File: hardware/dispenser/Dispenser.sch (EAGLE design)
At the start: 59 parts, among them J1 AVR_Prog, J2 RJ45-8PTH, Q1 NFET-SO8, Q2 NFET, Q3 NFET, Q4 NFET, U1 ATMEGA168, U10 HALL-EFFECT, U2 OPAMP-DUAL, U3 OPTO-TLP185, U4 MPX10DP, U5 VREG-5V-LDO-AP1117SOT89-3L, U6 WS2801, U7 HALL-EFFECT, U8 HALL-EFFECT, U9 HALL-EFFECT

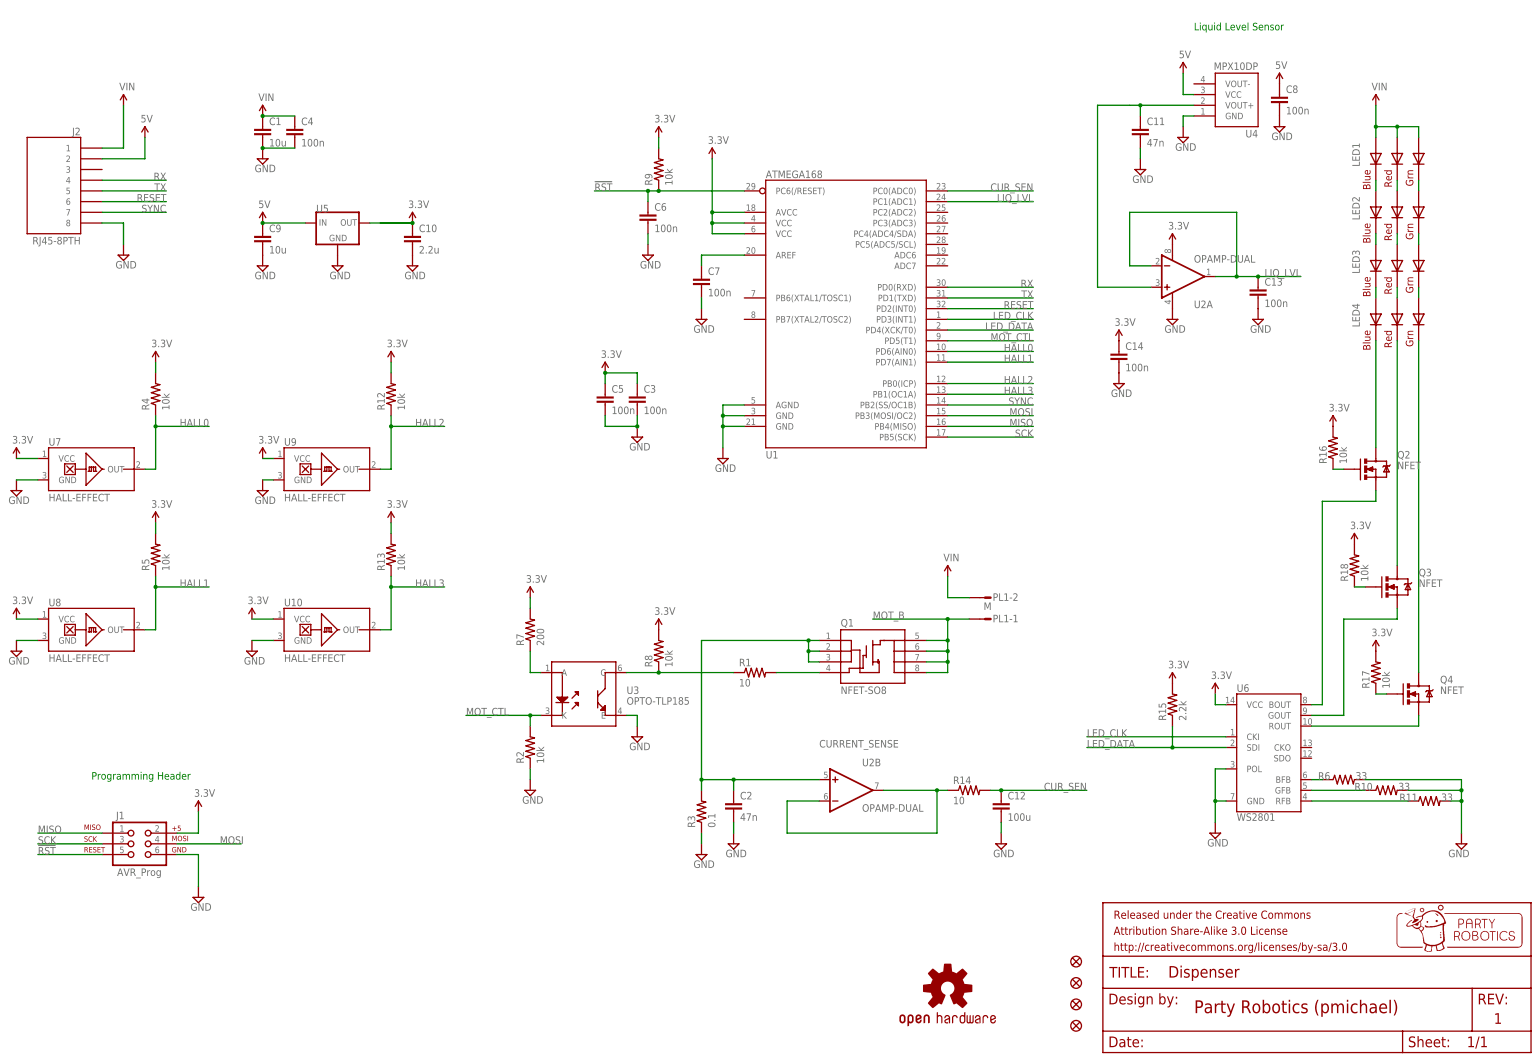
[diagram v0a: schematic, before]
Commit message: Updated Router Schematic with DS1307 and Accessory Port
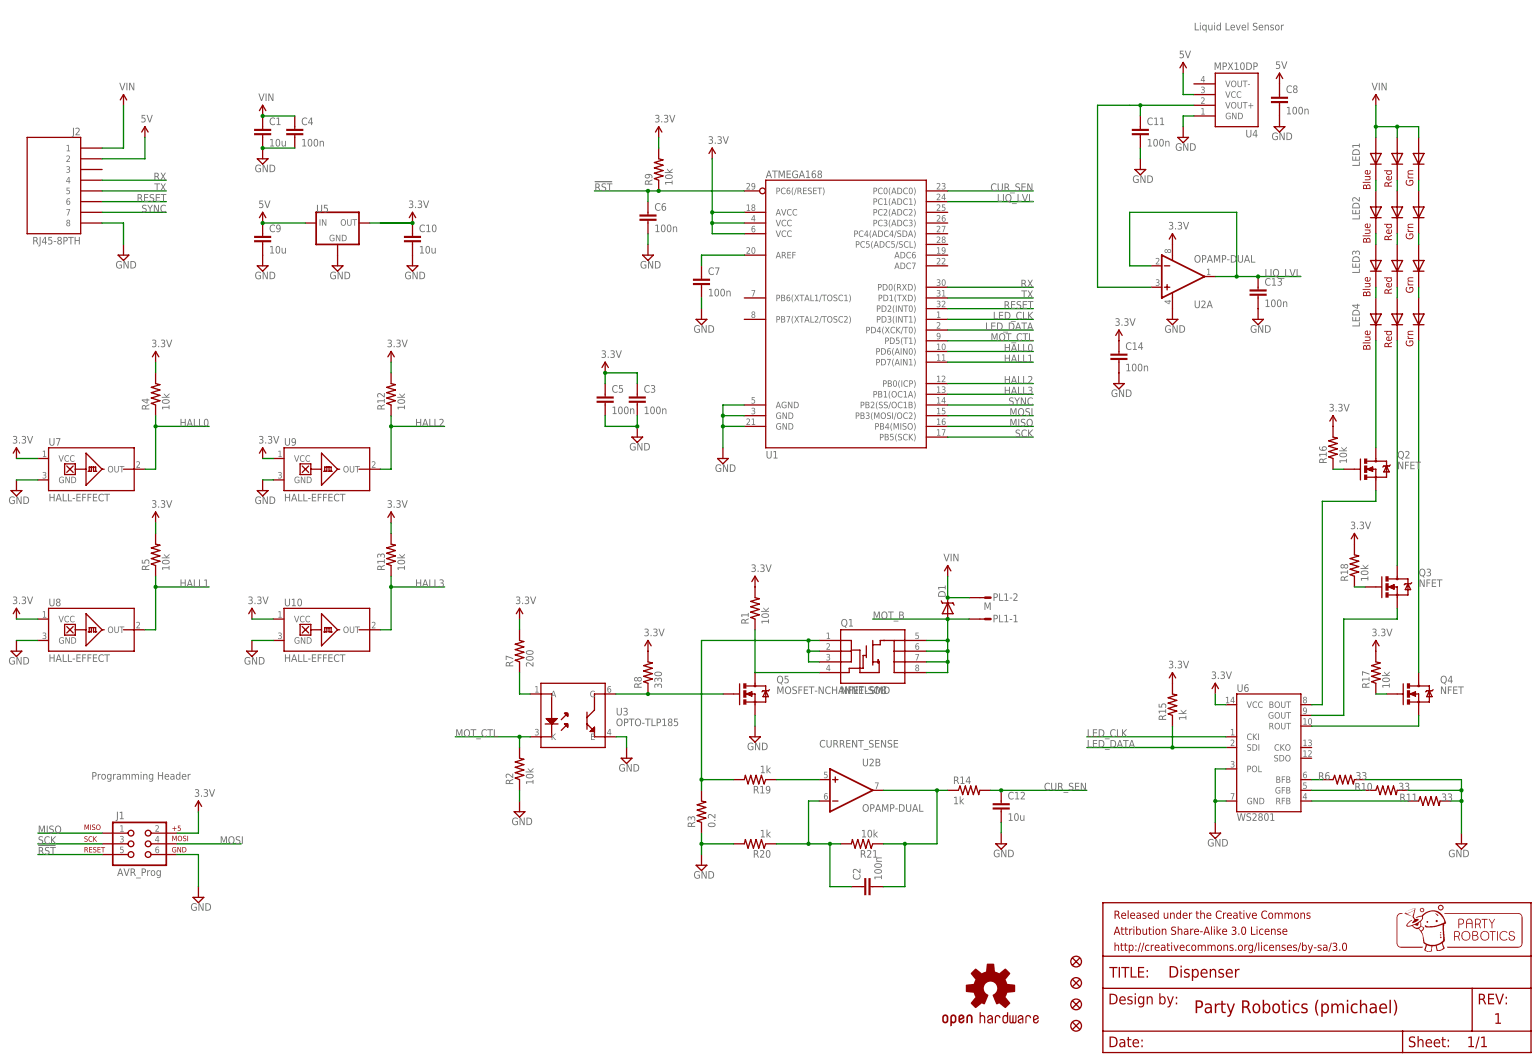
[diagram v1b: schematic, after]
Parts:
- added D1: (no value), pierre:B330A
- added Q5: MOSFET-NCHANNELSMD, SparkFun-DiscreteSemi:MOSFET-NCHANNELSMD
- added R19, R20: 1k, SparkFun-Resistors:RESISTOR0603-RES
- added R21: 10k, SparkFun-Resistors:RESISTOR0603-RES
- C10: value 2.2u -> 10u
- C11, C2: value 47n -> 100n
- C12: value 100u -> 10u
- R1: value 10 -> 10k
- R14: value 10 -> 1k
- R15: value 2.2k -> 1k
- R3: value 0.1 -> 0.2; device SparkFun-Resistors:RESISTOR0603-RES -> SparkFun-Resistors:RESISTOR0805-RES
- R8: value 10k -> 330
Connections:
- new net N$10: C2.1, R20.1, R21.2, U2B.-IN
- new net N$11: R19.1, U2B.+IN
- net 3.3V: now also R1.2; no longer U4.VCC
- net 5V: now also U4.VCC
- net CURRENT_SENSE: now also R19.2; no longer C2.1, U2B.+IN
- net GND: now also Q5.S, R20.2; no longer C2.2
- net MOT_B: now also D1.A
- net MOT_CUR: now also C2.2, R21.1; no longer U2B.-IN
- net N$31: now also Q5.G; no longer R1.1
- net N$9: now also Q5.D, R1.1; no longer R1.2
- net VIN: now also D1.C
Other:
- moved on the sheet: C2, R1, R2, R7, R8, U3

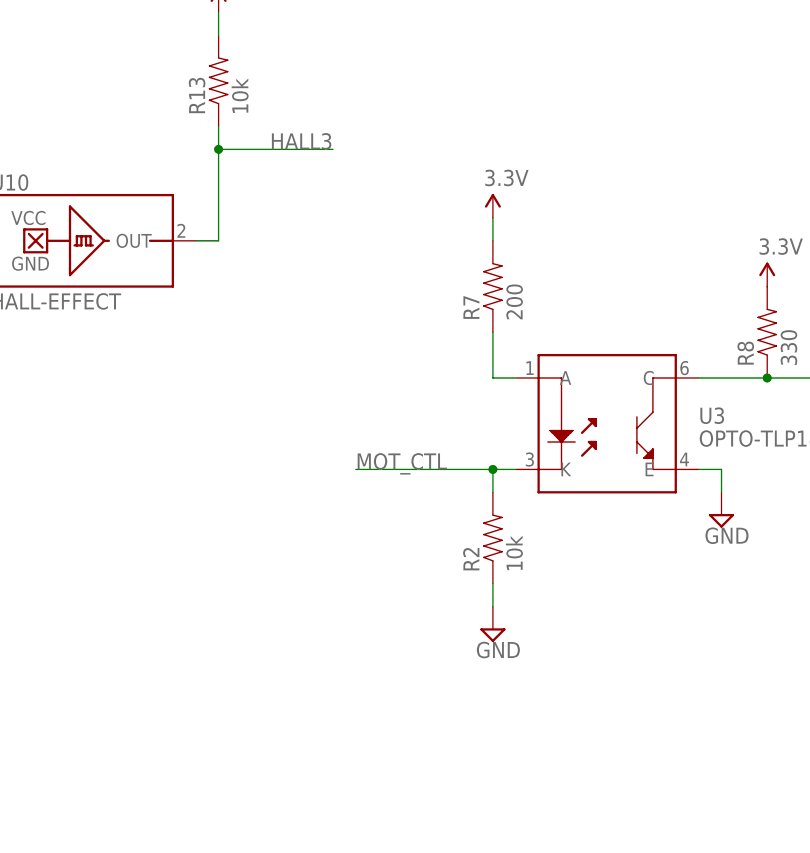
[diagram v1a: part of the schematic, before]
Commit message: Updated inputs to opto-isolator
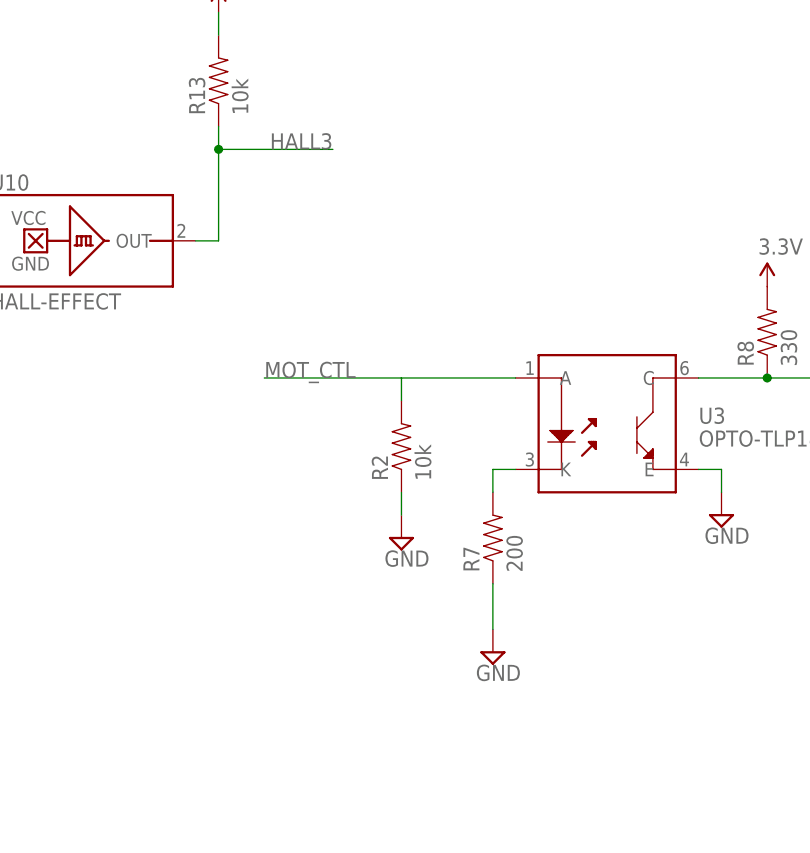
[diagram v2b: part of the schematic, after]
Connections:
- removed net N$35: R7.1, U3.A
- new net N$15: R7.2, U3.K
- net 3.3V: no longer R7.2
- net GND: now also R7.1
- net MOT_CTL: now also U3.A; no longer U3.K
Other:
- moved on the sheet: R2, R7
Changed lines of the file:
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@@
 <part name="P+9" library="SparkFun-Aesthetics" deviceset="3.3V" device="" value="5V"/>
 <part name="P+11" library="SparkFun-Aesthetics" deviceset="3.3V" device="" value="5V"/>
-<part name="P+10" library="SparkFun-Aesthetics" deviceset="3.3V" device=""/>
 <part name="P+12" library="SparkFun-Aesthetics" deviceset="3.3V" device=""/>
 <part name="P+14" library="SparkFun-Aesthetics" deviceset="3.3V" device=""/>
@@
 <part name="P+18" library="SparkFun-Aesthetics" deviceset="3.3V" device=""/>
 <part name="D1" library="pierre" deviceset="B330A" device=""/>
+<part name="SUPPLY22" library="supply2" deviceset="GND" device=""/>
 </parts>
 <sheets>
@@
 <instance part="U$14" gate="G$1" x="246.38" y="116.84"/>
 <instance part="U3" gate="G$1" x="157.48" y="83.82"/>
-<instance part="R7" gate="G$1" x="144.78" y="99.06" rot="R90"/>
+<instance part="R7" gate="G$1" x="144.78" y="71.12" rot="R90"/>
 <instance part="SUPPLY7" gate="GND" x="170.18" y="73.66"/>
 <instance part="R8" gate="G$1" x="175.26" y="93.98" rot="R90"/>
@@
 <instance part="P+9" gate="G$1" x="302.26" y="236.22"/>
 <instance part="P+11" gate="G$1" x="325.12" y="233.68"/>
-<instance part="P+10" gate="G$1" x="144.78" y="106.68"/>
 <instance part="P+12" gate="G$1" x="68.58" y="60.96"/>
 <instance part="P+14" gate="G$1" x="175.26" y="99.06"/>
@@
 <attribute name="VALUE" x="363.474" y="63.5" size="1.778" layer="96"/>
 </instance>
-<instance part="R2" gate="G$1" x="144.78" y="71.12" rot="R90"/>
-<instance part="SUPPLY4" gate="GND" x="144.78" y="60.96"/>
+<instance part="R2" gate="G$1" x="134.62" y="81.28" rot="R90"/>
+<instance part="SUPPLY4" gate="GND" x="134.62" y="71.12"/>
 <instance part="C12" gate="G$1" x="259.08" y="60.96"/>
 <instance part="SUPPLY5" gate="GND" x="259.08" y="53.34"/>
@@
 <instance part="P+18" gate="G$1" x="200.66" y="114.3"/>
 <instance part="D1" gate="G$1" x="246.38" y="109.22" rot="R90"/>
+<instance part="SUPPLY22" gate="GND" x="144.78" y="58.42"/>
 </instances>
 <busses>
@@
 <pinref part="R2" gate="G$1" pin="1"/>
 <pinref part="SUPPLY4" gate="GND" pin="GND"/>
-<wire x1="144.78" y1="66.04" x2="144.78" y2="63.5" width="0.1524" layer="91"/>
+<wire x1="134.62" y1="76.2" x2="134.62" y2="73.66" width="0.1524" layer="91"/>
 </segment>
 <segment>
@@
 <wire x1="200.66" y1="81.28" x2="200.66" y2="83.82" width="0.1524" layer="91"/>
 </segment>
+<segment>
+<pinref part="R7" gate="G$1" pin="1"/>
+<wire x1="144.78" y1="66.04" x2="144.78" y2="60.96" width="0.1524" layer="91"/>
+<pinref part="SUPPLY22" gate="GND" pin="GND"/>
+</segment>
 </net>
 <net name="5V" class="0">
@@
 </segment>
 </net>
-<net name="N$35" class="0">
-<segment>
-<pinref part="R7" gate="G$1" pin="1"/>
-<wire x1="144.78" y1="93.98" x2="144.78" y2="88.9" width="0.2032" layer="91"/>
-<pinref part="U3" gate="G$1" pin="A"/>
-<wire x1="144.78" y1="88.9" x2="147.32" y2="88.9" width="0.2032" layer="91"/>
-</segment>
-</net>
 <net name="TX" class="0">
 <segment>
@@
 </segment>
 <segment>
-<pinref part="R7" gate="G$1" pin="2"/>
-<pinref part="P+10" gate="G$1" pin="3.3V"/>
-<wire x1="144.78" y1="106.68" x2="144.78" y2="104.14" width="0.1524" layer="91"/>
-</segment>
-<segment>
 <pinref part="J1" gate="G$1" pin="2"/>
 <wire x1="63.5" y1="55.88" x2="68.58" y2="55.88" width="0.2032" layer="91"/>
@@
 <net name="MOT_CTL" class="0">
 <segment>
-<pinref part="U3" gate="G$1" pin="K"/>
-<label x="129.54" y="78.74" size="1.778" layer="95"/>
-<wire x1="147.32" y1="78.74" x2="144.78" y2="78.74" width="0.2032" layer="91"/>
-<wire x1="144.78" y1="76.2" x2="144.78" y2="78.74" width="0.2032" layer="91"/>
-<wire x1="144.78" y1="78.74" x2="129.54" y2="78.74" width="0.2032" layer="91"/>
+<label x="119.38" y="88.9" size="1.778" layer="95"/>
+<wire x1="134.62" y1="86.36" x2="134.62" y2="88.9" width="0.2032" layer="91"/>
+<wire x1="134.62" y1="88.9" x2="119.38" y2="88.9" width="0.2032" layer="91"/>
 <pinref part="R2" gate="G$1" pin="2"/>
-<junction x="144.78" y="78.74"/>
+<pinref part="U3" gate="G$1" pin="A"/>
+<wire x1="134.62" y1="88.9" x2="147.32" y2="88.9" width="0.1524" layer="91"/>
 </segment>
 <segment>
@@
 </segment>
 </net>
+<net name="N$15" class="0">
+<segment>
+<pinref part="R7" gate="G$1" pin="2"/>
+<wire x1="144.78" y1="76.2" x2="144.78" y2="78.74" width="0.1524" layer="91"/>
+<pinref part="U3" gate="G$1" pin="K"/>
+<wire x1="144.78" y1="78.74" x2="147.32" y2="78.74" width="0.1524" layer="91"/>
+</segment>
+</net>

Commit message: Dispener updates
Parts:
- PL1: value M -> Motor Connector
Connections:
- net CURRENT_SENSE renamed 1/4W
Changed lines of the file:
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@@
 <part name="Q3" library="SparkFun-DiscreteSemi" deviceset="MOSFET-NCHANNEL" device="SMD" value="NFET"/>
 <part name="Q4" library="SparkFun-DiscreteSemi" deviceset="MOSFET-NCHANNEL" device="SMD" value="NFET"/>
-<part name="PL1" library="con-hirose-df3" deviceset="DF3-02" device="P" value="M"/>
+<part name="PL1" library="con-hirose-df3" deviceset="DF3-02" device="P" value="Motor Connector"/>
 <part name="U5" library="pierre" deviceset="VREG-5V-LDO-AP1117" device="SOT89-3L"/>
 <part name="C9" library="SparkFun-Passives" deviceset="CAP" device="0603-CAP" value="10u"/>
@@
 <instance part="Q3" gate="G$1" x="353.06" y="114.3"/>
 <instance part="Q4" gate="G$1" x="358.14" y="88.9"/>
-<instance part="PL1" gate="-1" x="256.54" y="106.68" rot="MR0"/>
-<instance part="PL1" gate="-2" x="256.54" y="111.76" rot="MR0"/>
+<instance part="PL1" gate="-1" x="256.54" y="106.68" smashed="yes" rot="MR0">
+<attribute name="NAME" x="257.048" y="107.696" size="1.778" layer="95" rot="MR180"/>
+<attribute name="VALUE" x="269.494" y="108.839" size="1.778" layer="96" rot="MR0"/>
+</instance>
+<instance part="PL1" gate="-2" x="256.54" y="111.76" smashed="yes" rot="MR0">
+<attribute name="NAME" x="257.048" y="112.776" size="1.778" layer="95" rot="MR180"/>
+</instance>
 <instance part="U5" gate="G$1" x="101.6" y="200.66" smashed="yes">
 <attribute name="NAME" x="96.52" y="203.2" size="1.778" layer="95"/>
@@
 <junction x="246.38" y="99.06"/>
 <junction x="246.38" y="96.52"/>
-<label x="228.6" y="106.68" size="1.778" layer="95"/>
-<wire x1="246.38" y1="106.68" x2="228.6" y2="106.68" width="0.2032" layer="91"/>
 <wire x1="246.38" y1="101.6" x2="246.38" y2="106.68" width="0.1524" layer="91"/>
 <pinref part="PL1" gate="-1" pin="S"/>
@@
 </segment>
 </net>
-<net name="CURRENT_SENSE" class="0">
+<net name="1/4W" class="0">
 <segment>
 <label x="215.9" y="76.2" size="1.778" layer="95"/>
@@
 <wire x1="195.58" y1="68.58" x2="187.96" y2="68.58" width="0.1524" layer="91"/>
 <junction x="187.96" y="68.58"/>
+<label x="177.8" y="60.96" size="1.778" layer="95"/>
 </segment>
 </net>
